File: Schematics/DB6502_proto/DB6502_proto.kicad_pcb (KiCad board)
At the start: 2 copper layers, 133.3 x 105.4 mm, 55 parts, among them J1 System Bus, J10 AVR-ISP-6, J2 Controls, J3 Debug UART, J4 I/O Bus, J5 USB_B, SW1 Reset, U1 DS1813, U2 65C02S, U3 62256, U4 ATmega644PA-PU, U5 62256, U6 74AC138, U7 28C256, U8 22V10C, U9 FT230XS, Y1 20MHz

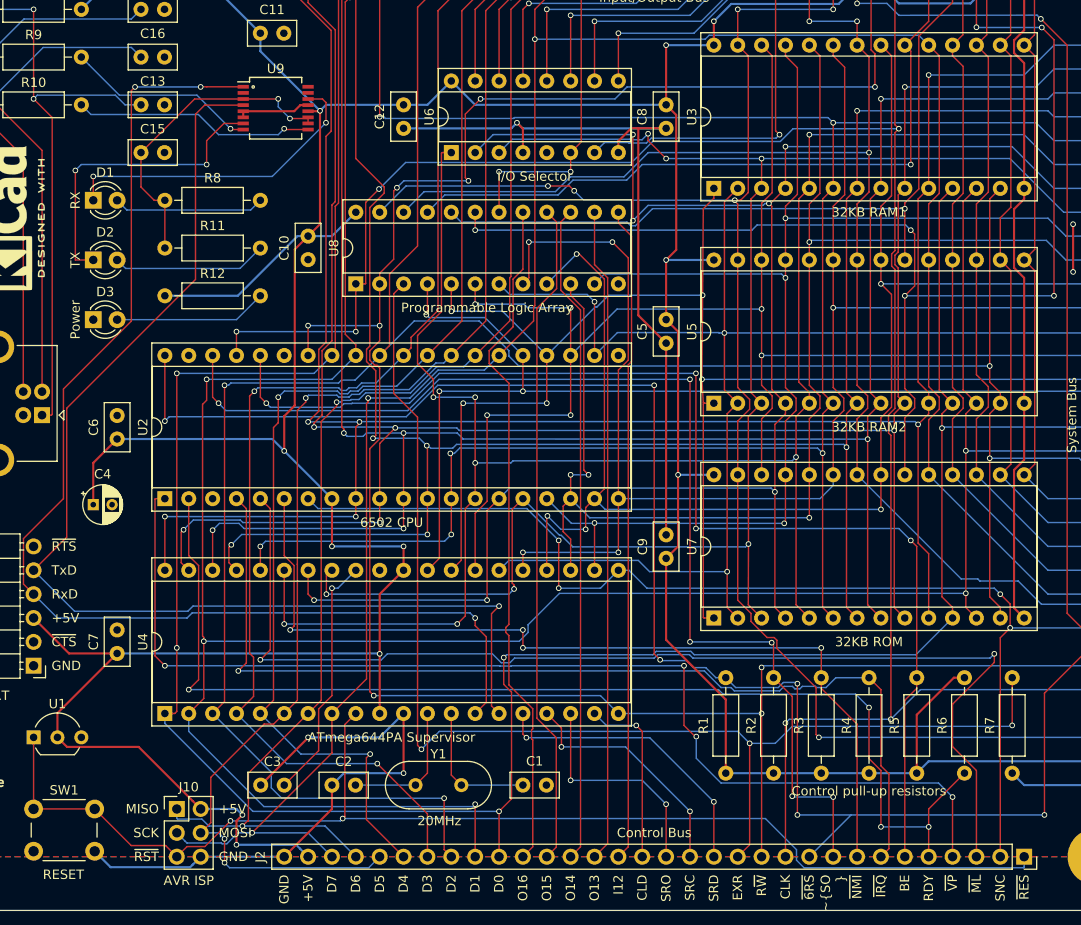
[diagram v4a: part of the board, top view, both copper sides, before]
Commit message: AVR ISP connections cleanup
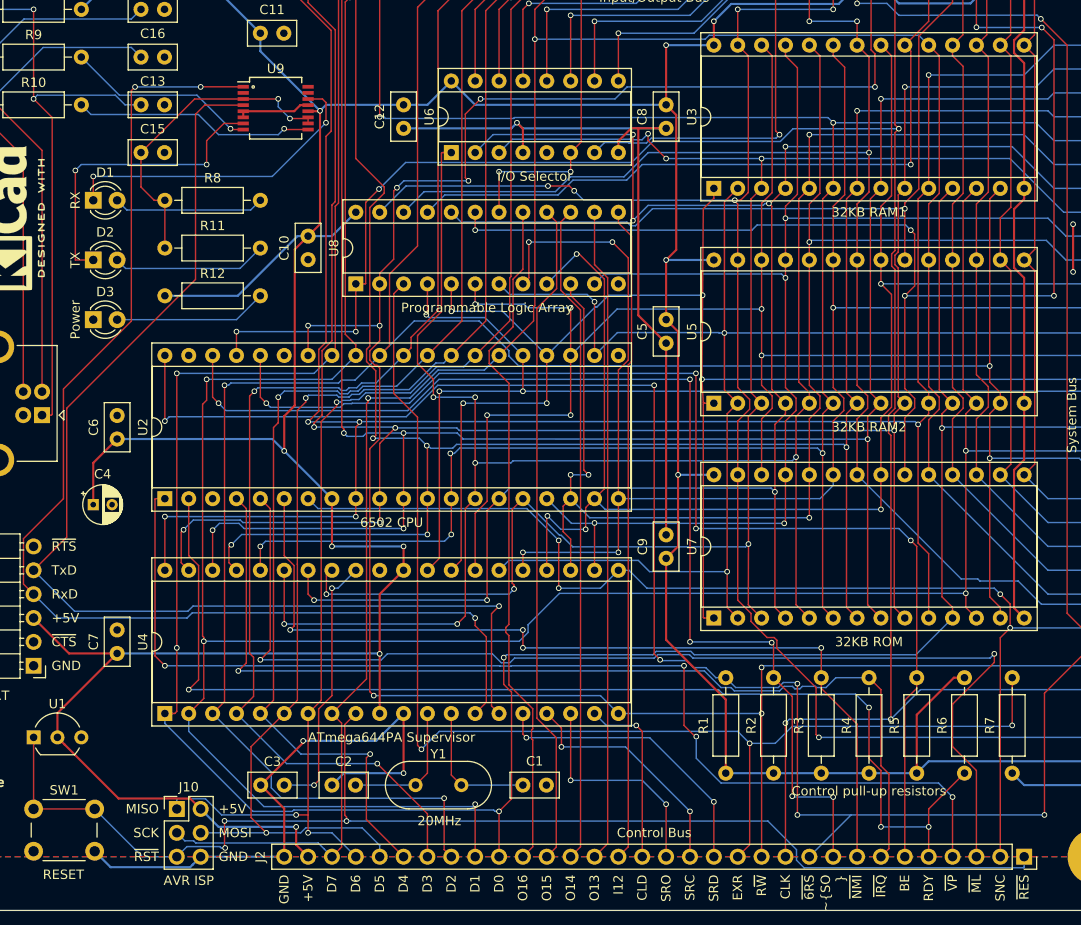
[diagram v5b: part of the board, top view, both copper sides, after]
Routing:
- net d5: track 258.3 -> 254.8 mm, vias 3 -> 2
- net d6: track 252.5 -> 250.4 mm, vias 2 -> 3
- net ~RES: track 132.5 -> 134.5 mm, vias 2 -> 3
- net Net-(C3-Pad2): track 26.4 -> 28.2 mm, vias 1 -> 2
- net +5V: track 470.4 -> 468.7 mm, vias 11 -> 10
- net d7: track 242.7 -> 241.6 mm, vias 3 -> 2
- net GND: track 241.5 -> 240.6 mm

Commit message: Working on the second PCB
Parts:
- removed REF**: OSHW-Logo_7.5x8mm_SilkScreen, Symbol:OSHW-Logo_7.5x8mm_SilkScreen
- removed REF**: KiCad-Logo2_6mm_SilkScreen, Symbol:KiCad-Logo2_6mm_SilkScreen
- removed REF** (x4): MountingHole_3mm_Pad, MountingHole:MountingHole_3mm_Pad
- added C17: 0,1uF, Capacitor_SMD:C_0805_2012Metric_Pad1.15x1.40mm_HandSolder, B.Cu at (449.6, 148.8)
- added C18: 22pF, Capacitor_THT:C_Disc_D5.0mm_W2.5mm_P2.50mm, F.Cu at (337.8, 83.8)
- added C19: 22pF, Capacitor_THT:C_Disc_D5.0mm_W2.5mm_P2.50mm, F.Cu at (360.7, 83.8)
- added C20: 0,1uF, Capacitor_SMD:C_0805_2012Metric_Pad1.15x1.40mm_HandSolder, B.Cu at (96.8, 121.6)
- added C21: 0,1uF, Capacitor_SMD:C_0805_2012Metric_Pad1.15x1.40mm_HandSolder, B.Cu at (62.2, 172.7)
- added C22: 0,1uF, Capacitor_SMD:C_0805_2012Metric_Pad1.15x1.40mm_HandSolder, B.Cu at (62.2, 168.9)
- added C23: 0,1uF, Capacitor_SMD:C_0805_2012Metric_Pad1.15x1.40mm_HandSolder, B.Cu at (363.2, 163.8)
- added C24: 0,1uF, Capacitor_SMD:C_0805_2012Metric_Pad1.15x1.40mm_HandSolder, B.Cu at (437.1, 92.7)
- added C25: 0,1uF, Capacitor_SMD:C_0805_2012Metric_Pad1.15x1.40mm_HandSolder, B.Cu at (363.2, 179.1)
- added C26: 0,1uF, Capacitor_SMD:C_0805_2012Metric_Pad1.15x1.40mm_HandSolder, B.Cu at (96.8, 125.7)
- added C27: 0,1uF, Capacitor_SMD:C_0805_2012Metric_Pad1.15x1.40mm_HandSolder, B.Cu at (378.5, 133.3)
- added C28: 22pF, Capacitor_THT:C_Disc_D5.0mm_W2.5mm_P2.50mm, F.Cu at (454.7, 93.9)
- added C29: 22pF, Capacitor_THT:C_Disc_D5.0mm_W2.5mm_P2.50mm, F.Cu at (454.7, 116.8)
- added C30: 0,1uF, Capacitor_SMD:C_0805_2012Metric_Pad1.15x1.40mm_HandSolder, B.Cu at (378.5, 118.1)
- added D4: BLINK, LED_THT:LED_D3.0mm, F.Cu at (387.4, 143.5)
- added J11: VIA Ports, Connector_PinSocket_2.54mm:PinSocket_1x20_P2.54mm_Vertical, F.Cu at (179.5, 90.8)
- added J12: Power plug, Connector_BarrelJack:BarrelJack_Horizontal, F.Cu at (395.9, 72.4)
- added J6: UART B, Connector_PinHeader_2.54mm:PinHeader_1x06_P2.54mm_Horizontal, F.Cu at (433.1, 68.6)
- added J7: I/O Bus, Connector_PinSocket_2.54mm:PinSocket_1x32_P2.54mm_Vertical, F.Cu at (24.8, 31.0)
- added J8: System Bus, Connector_PinSocket_2.54mm:PinSocket_1x32_P2.54mm_Vertical, F.Cu at (20.2, 31.0)
- added J9: Clock divider, Connector_PinHeader_2.54mm:PinHeader_2x03_P2.54mm_Vertical, F.Cu at (388.6, 152.4)
- added JP1: PLD CLK Selector, Connector_PinSocket_2.54mm:PinSocket_1x03_P2.54mm_Vertical, F.Cu at (378.5, 106.7)
- added JP10: Blink, Connector_PinHeader_2.54mm:PinHeader_2x01_P2.54mm_Vertical, F.Cu at (395.0, 144.8)
- added JP2: PLD ~WR, Connector_PinHeader_2.54mm:PinHeader_1x02_P2.54mm_Vertical, F.Cu at (381.0, 83.8)
- added JP3: PLD ~RD, Connector_PinHeader_2.54mm:PinHeader_1x02_P2.54mm_Vertical, F.Cu at (386.1, 83.8)
- added JP4: PLD RDY, Connector_PinHeader_2.54mm:PinHeader_1x02_P2.54mm_Vertical, F.Cu at (391.2, 83.8)
- added JP5: PLD DBG_WAIT, Connector_PinHeader_2.54mm:PinHeader_1x02_P2.54mm_Vertical, F.Cu at (396.2, 83.8)
- added JP6: PLD WS_DISABLE, Connector_PinHeader_2.54mm:PinHeader_1x02_P2.54mm_Vertical, F.Cu at (401.3, 83.8)
- added JP7: PLD RDY_M1F, Connector_PinHeader_2.54mm:PinHeader_1x02_P2.54mm_Vertical, F.Cu at (406.4, 83.8)
- added JP8: PLD RDY_M2F, Connector_PinHeader_2.54mm:PinHeader_1x02_P2.54mm_Vertical, F.Cu at (411.5, 83.8)
- added JP9: Debug RxD, Connector_PinHeader_2.54mm:PinHeader_2x01_P2.54mm_Vertical, F.Cu at (39.6, 158.2)
- added R13: 27, Resistor_THT:R_Axial_DIN0207_L6.3mm_D2.5mm_P10.16mm_Horizontal, F.Cu at (46.6, 52.1)
- added R14: 27, Resistor_THT:R_Axial_DIN0207_L6.3mm_D2.5mm_P10.16mm_Horizontal, F.Cu at (65.5, 48.1)
- added R15: 220, Resistor_THT:R_Axial_DIN0207_L6.3mm_D2.5mm_P10.16mm_Horizontal, F.Cu at (38.9, 163.2)
- added R16: 220, Resistor_THT:R_Axial_DIN0207_L6.3mm_D2.5mm_P10.16mm_Horizontal, F.Cu at (62.4, 143.7)
- added R17: 4K7, Resistor_THT:R_Axial_DIN0207_L6.3mm_D2.5mm_P10.16mm_Horizontal, F.Cu at (62.4, 147.7)
- added R18: 0R, Resistor_THT:R_Axial_DIN0207_L6.3mm_D2.5mm_P10.16mm_Horizontal, F.Cu at (455.9, 149.9)
- added R19: 220, Resistor_THT:R_Axial_DIN0207_L6.3mm_D2.5mm_P10.16mm_Horizontal, F.Cu at (361.9, 137.2)
- added RV1: 10K, Potentiometer_THT:Potentiometer_Piher_PT-10-V10_Vertical, F.Cu at (386.1, 181.6)
- added TP1: TestPoint, TestPoint:TestPoint_Keystone_5005-5009_Compact, F.Cu at (228.2, 81.7)
- added TP2: TestPoint, TestPoint:TestPoint_Keystone_5005-5009_Compact, F.Cu at (234.8, 76.6)
- added U10: FT230XS, Package_SO:SSOP-16_5.3x6.2mm_P0.65mm, F.Cu at (55.1, 169.2)
- added U11: 74HC595, Package_DIP:DIP-16_W7.62mm_Socket, F.Cu at (378.5, 121.9)
- added U12: 74HC157, Package_DIP:DIP-16_W7.62mm_Socket, F.Cu at (363.2, 152.4)
- added U13: ATmega644PA-PU, Package_DIP:DIP-40_W15.24mm_Socket, F.Cu at (322.6, 106.7)
- added U14: 74AC74, Package_DIP:DIP-14_W7.62mm_Socket, F.Cu at (386.1, 167.6)
- added U15: DS1813, Package_TO_SOT_THT:TO-92_Inline_Wide, F.Cu at (322.6, 73.7)
- added U16: 74AC74, Package_DIP:DIP-14_W7.62mm_Socket, F.Cu at (363.2, 167.6)
- added U17: 74AC08, Package_DIP:DIP-14_W7.62mm_Socket, F.Cu at (403.9, 129.5)
- added U18: SC26C92, Package_LCC:PLCC-44_THT-Socket, F.Cu at (438.1, 97.8)
- added U19: 65C22S, Package_DIP:DIP-40_W15.24mm_Socket, F.Cu at (401.3, 152.4)
- added X1: 8MHz, Oscillator:Oscillator_DIP-14, F.Cu at (363.2, 182.9)
- added Y2: 3,6864MHz, Crystal:Crystal_HC49-U_Vertical, F.Cu at (454.7, 101.6)
- C1, C2: value 22pF -> 0,1uF; footprint Capacitor_THT:C_Disc_D5.0mm_W2.5mm_P2.50mm -> Capacitor_SMD:C_0805_2012Metric_Pad1.15x1.40mm_HandSolder; moved to B.Cu
- C10: value 100nF -> 10uF; footprint Capacitor_THT:C_Disc_D5.0mm_W2.5mm_P2.50mm -> Capacitor_THT:CP_Radial_D4.0mm_P2.00mm
- C11: value 100nF -> 10nF
- C12: value 100nF -> 47pF
- C13: value 10nF -> 47pF
- C14, C16: value 47pF -> 0,1uF; footprint Capacitor_THT:C_Disc_D5.0mm_W2.5mm_P2.50mm -> Capacitor_SMD:C_0805_2012Metric_Pad1.15x1.40mm_HandSolder; moved to B.Cu
- C15, C3, C5, C6, C8, C9: value 100nF -> 0,1uF; footprint Capacitor_THT:C_Disc_D5.0mm_W2.5mm_P2.50mm -> Capacitor_SMD:C_0805_2012Metric_Pad1.15x1.40mm_HandSolder; moved to B.Cu
- C4: value 10uF -> 0,1uF; footprint Capacitor_THT:CP_Radial_D4.0mm_P2.00mm -> Capacitor_SMD:C_0805_2012Metric_Pad1.15x1.40mm_HandSolder; moved to B.Cu
- C7: value 100nF -> 22pF
- D1: value RX -> PWR
- D2: value TX -> D_TX
- D3: value PWR -> D_RX
- J1: value System Bus -> Controls
- J10: value AVR-ISP-6 -> LCD Port; footprint Connector_PinHeader_2.54mm:PinHeader_2x03_P2.54mm_Vertical -> Connector_PinSocket_2.54mm:PinSocket_1x16_P2.54mm_Vertical
- J2: value Controls -> AVR ISP; footprint Connector_PinSocket_2.54mm:PinSocket_1x32_P2.54mm_Vertical -> Connector_PinHeader_2.54mm:PinHeader_2x03_P2.54mm_Vertical
- J3: value Debug UART -> Debug USB; footprint Connector_PinHeader_2.54mm:PinHeader_1x06_P2.54mm_Horizontal -> Connector_USB:USB_B_OST_USB-B1HSxx_Horizontal
- J4: value I/O Bus -> Debug UART; footprint Connector_PinSocket_2.54mm:PinSocket_1x32_P2.54mm_Vertical -> Connector_PinHeader_2.54mm:PinHeader_1x06_P2.54mm_Horizontal
- J5: value USB_B -> UART A; footprint Connector_USB:USB_B_OST_USB-B1HSxx_Horizontal -> Connector_PinHeader_2.54mm:PinHeader_1x06_P2.54mm_Horizontal
- R1: value 4K7 -> 470
- R10, R9: value 27 -> 4K7
- R11, R12, R8: value 220 -> 4K7
- R5: value 4K7 -> 220
- U1: value DS1813 -> 62256; footprint Package_TO_SOT_THT:TO-92_Inline_Wide -> Package_DIP:DIP-28_W15.24mm_Socket
- U2: value 65C02S -> 71256; footprint Package_DIP:DIP-40_W15.24mm_Socket -> Package_DIP:DIP-28_W7.62mm_Socket
- U3: value 62256 -> 71256; footprint Package_DIP:DIP-28_W15.24mm_Socket -> Package_DIP:DIP-28_W7.62mm_Socket
- U4: value ATmega644PA-PU -> 65C02S
- U5: value 62256 -> 74AC74; footprint Package_DIP:DIP-28_W15.24mm_Socket -> Package_DIP:DIP-14_W7.62mm_Socket
- U7: value 28C256 -> 22V10C; footprint Package_DIP:DIP-28_W15.24mm_Socket -> Package_DIP:DIP-24_W7.62mm_Socket
- U8: value 22V10C -> 74AC04; footprint Package_DIP:DIP-24_W7.62mm_Socket -> Package_DIP:DIP-14_W7.62mm_Socket
- U9: value FT230XS -> 74HC21; footprint Package_SO:SSOP-16_5.3x6.2mm_P0.65mm -> Package_DIP:DIP-14_W7.62mm_Socket
- moved C16 376.5 mm to (426.7, 125.7), turned to 270 degrees
- moved J5 359.8 mm to (412.8, 68.6), turned to 90 degrees
- moved J10 353.3 mm to (416.6, 160.0), turned to 90 degrees
- moved C15 346.7 mm to (386.1, 163.8), turned to 270 degrees
- moved U6 343.0 mm to (426.7, 129.5)
- moved U8 334.6 mm to (419.1, 86.4)
- moved C14 325.5 mm to (363.2, 148.6), turned to 270 degrees
- moved D1 325.4 mm to (382.3, 73.1)
- moved C10 324.9 mm to (405.1, 72.4), turned to 0 degrees
- moved C6 318.7 mm to (378.5, 95.2), turned to 270 degrees
- moved U9 318.5 mm to (378.5, 137.2), turned to 90 degrees
- moved J3 316.7 mm to (368.3, 73.7), turned to 90 degrees
- moved C8 295.2 mm to (403.9, 110.5)
- moved C9 288.1 mm to (403.9, 125.7), turned to 270 degrees
- moved U5 284.0 mm to (403.9, 114.3)
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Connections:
- C1 pad 1: GND -> +5V
- C1 pad 2: Net-(C1-Pad2) -> GND
- C11 pad 1: +5V -> Net-(C11-Pad1)
- C12 pad 1: +5V -> Net-(C12-Pad1)
- C14 pad 1: Net-(C14-Pad1) -> +5V
- C15 pad 1: Net-(C15-Pad1) -> +5V
- C16 pad 1: Net-(C16-Pad1) -> +5V
- C2 pad 1: GND -> +5V
- C2 pad 2: Net-(C2-Pad2) -> GND
- C3 pad 1: GND -> +5V
- C3 pad 2: Net-(C3-Pad2) -> GND
- C7 pad 1: +5V -> 6502_RDY_IN
- C7 pad 2: GND -> 6502_RDY
- D1 pad 1: ~RXLED -> GND
- D2 pad 1: ~TXLED -> ~DBG_TXLED
- D3 pad 1: GND -> ~DBG_RXLED
- FB1 pad 2: Net-(C13-Pad1) -> Net-(C11-Pad1)
- J1 pad 1: a0 -> ~RES
- J1 pad 10: a9 -> ~6502_RES
- J1 pad 11: a10 -> 6502_CLK
- J1 pad 12: a11 -> R~W
- J1 pad 13: a12 -> EXRAM
- J1 pad 14: a13 -> SR_DAT
- J1 pad 15: a14 -> SR_CLK
- J1 pad 16: a15 -> SR_OUT
- J1 pad 17: d0 -> DBG_CLK
- J1 pad 18: d1 -> RDY_M1F
- J1 pad 19: d2 -> RDY_M2F
- J1 pad 2: a1 -> SYNC
- J1 pad 20: d3 -> WS_DISABLE
- J1 pad 21: d4 -> DBG_WAIT
- J1 pad 22: d5 -> 6502_RDY
- J1 pad 23: d6 -> d0
- J1 pad 24: d7 -> d1
- J1 pad 25: SYNC -> d2
- J1 pad 26: ~6502_RES -> d3
- J1 pad 27: R~W -> d4
- J1 pad 28: CLK -> d5
- J1 pad 29: ~OE -> d6
- J1 pad 3: a2 -> ~ML
- J1 pad 30: ~WE -> d7
- J1 pad 4: a3 -> ~VP
- J1 pad 5: a4 -> 6502_RDY
- J1 pad 6: a5 -> BE
- J1 pad 7: a6 -> ~IRQ
- J1 pad 8: a7 -> ~NMI
- J1 pad 9: a8 -> ~SO
- J10 pad 1: d6 -> GND
- J10 pad 3: d7 -> Net-(J10-Pad3)
- J10 pad 4: d5 -> /serial/v1pb1
- J10 pad 5: ~RES -> /serial/v1pb2
- J10 pad 6: GND -> /serial/v1pb3
- J2 pad 1: ~RES -> d6
- J2 pad 2: SYNC -> +5V
- J2 pad 3: ~ML -> d7
- J2 pad 4: ~VP -> d5
- J2 pad 5: RDY -> ~RES
- J2 pad 6: BE -> GND
- J3 pad 1: GND -> Net-(C11-Pad1)
- J3 pad 2: GND -> Net-(C13-Pad1)
- J3 pad 3: +5V -> Net-(C12-Pad1)
- J3 pad 4: RxD_DBG -> GND
- J3 pad 5: TxD_DBG -> Net-(J3-Pad5)
- J4 pad 1: a0 -> GND
- J4 pad 2: a1 -> GND
- J4 pad 3: a2 -> Net-(J4-Pad3)
- J4 pad 4: a3 -> DBG_RxD
- J4 pad 5: a4 -> DBG_TxD
- J4 pad 6: d0 -> Net-(J4-Pad6)
- J5 pad 1: Net-(C13-Pad1) -> GND
- J5 pad 2: Net-(C16-Pad1) -> UART_A_~RTS
- J5 pad 3: Net-(C14-Pad1) -> Net-(J5-Pad3)
- J5 pad 4: GND -> UART_A_RxD
- J5 pad 5: Net-(J5-Pad5) -> UART_A_TxD
- R1 pad 1: +5V -> 6502_RDY_IN
- R1 pad 2: ~6502_RES -> 6502_RDY
- R10 pad 1: Net-(C16-Pad1) -> +5V
- R10 pad 2: USBD- -> BE
- R11 pad 1: Net-(C15-Pad1) -> 6502_RDY
- R11 pad 2: Net-(D2-Pad2) -> +5V
- R12 pad 1: +5V -> GND
- R12 pad 2: Net-(D3-Pad2) -> EXRAM
- R2 pad 2: ~SO -> ~EXT_IRQ
- R3 pad 2: ~NMI -> ~UART_IRQ
- R4 pad 2: ~IRQ -> ~VIA2_IRQ
- R5 pad 2: BE -> Net-(D1-Pad2)
- R6 pad 1: RDY -> +5V
- R6 pad 2: +5V -> ~6502_RES
- R7 pad 1: GND -> +5V
- R7 pad 2: EXRAM -> ~SO
- R8 pad 1: Net-(C15-Pad1) -> +5V
- R8 pad 2: Net-(D1-Pad2) -> ~NMI
- R9 pad 1: Net-(C14-Pad1) -> +5V
- R9 pad 2: USBD+ -> ~IRQ
- U1 pad 1: ~RES -> a14
- U1 pad 2: +5V -> a12
- U1 pad 3: GND -> a7
- U2 pad 1: ~VP -> a14
- U2 pad 10: a1 -> a0
- U2 pad 11: a2 -> d0
- U2 pad 12: a3 -> d1
- U2 pad 13: a4 -> d2
- U2 pad 14: a5 -> GND
- U2 pad 15: a6 -> d3
- U2 pad 16: a7 -> d4
- U2 pad 17: a8 -> d5
- U2 pad 18: a9 -> d6
- U2 pad 19: a10 -> d7
- U2 pad 2: RDY -> a12
- U2 pad 20: a11 -> RAM2_~CS
- U2 pad 21: GND -> a10
- U2 pad 22: a12 -> ~RD
- U2 pad 23: a13 -> a11
- U2 pad 24: a14 -> a9
- U2 pad 25: a15 -> a8
- U2 pad 26: d7 -> a13
- U2 pad 27: d6 -> ~WR
- U2 pad 28: d5 -> +5V
- U2 pad 3: Net-(U2-Pad3) -> a7
- U2 pad 4: ~IRQ -> a6
- U2 pad 5: ~ML -> a5
- U2 pad 6: ~NMI -> a4
- U2 pad 7: SYNC -> a3
- U2 pad 8: +5V -> a2
- U2 pad 9: a0 -> a1
- U3 pad 20: RAM1_~CS -> ROM_~CS
- U3 pad 22: ~OE -> ~RD
- U3 pad 27: ~WE -> ~WR
- U4 pad 1: d0 -> ~VP
- U4 pad 10: +5V -> a1
- U4 pad 11: GND -> a2
- U4 pad 12: Net-(C2-Pad2) -> a3
- U4 pad 13: Net-(C1-Pad2) -> a4
- U4 pad 14: RxD_DBG -> a5
- U4 pad 15: TxD_DBG -> a6
- U4 pad 16: SR_DAT -> a7
- U4 pad 17: SR_CLK -> a8
- U4 pad 18: SR_OUT -> a9
- U4 pad 19: CLK_DBG -> a10
- U4 pad 2: d1 -> 6502_RDY_IN
- U4 pad 20: R~W -> a11
- U4 pad 21: SYNC -> GND
- U4 pad 22: a8 -> a12
- U4 pad 23: a9 -> a13
- U4 pad 24: a10 -> a14
- U4 pad 25: a11 -> a15
- U4 pad 26: a12 -> d7
- U4 pad 27: a13 -> d6
- U4 pad 28: a14 -> d5
- U4 pad 29: a15 -> d4
- U4 pad 3: d2 -> Net-(U4-Pad3)
- U4 pad 30: +5V -> d3
- U4 pad 31: GND -> d2
- U4 pad 32: Net-(C3-Pad2) -> d1
- U4 pad 33: a7 -> d0
- U4 pad 34: a6 -> R~W
- U4 pad 35: a5 -> Net-(U4-Pad35)
- U4 pad 36: a4 -> BE
- U4 pad 37: a3 -> 6502_CLK
- U4 pad 38: a2 -> ~SO
- U4 pad 39: a1 -> Net-(U4-Pad39)
- U4 pad 4: d3 -> ~IRQ
- U4 pad 40: a0 -> ~6502_RES
- U4 pad 5: d4 -> ~ML
- U4 pad 6: d5 -> ~NMI
- U4 pad 7: d6 -> SYNC
- U4 pad 8: d7 -> +5V
- U4 pad 9: ~RES -> a0
- U5 pad 1: a14 -> +5V
- U5 pad 10: a0 -> ~6502_RES
- U5 pad 11: d0 -> ~6502_CLK
- U5 pad 12: d1 -> RDY_M1F
- U5 pad 13: d2 -> +5V
- U5 pad 14: GND -> +5V
- U5 pad 2: a12 -> 6502_RDY
- U5 pad 3: a7 -> ~6502_CLK
- U5 pad 4: a6 -> ~6502_RES
- U5 pad 5: a5 -> RDY_M1F
- U5 pad 6: a4 -> Net-(U5-Pad6)
- U5 pad 7: a3 -> GND
- U5 pad 8: a2 -> Net-(U5-Pad8)
- U5 pad 9: a1 -> RDY_M2F
- U7 pad 1: a14 -> PLD_CLK
- U7 pad 10: a0 -> a9
- U7 pad 11: d0 -> a8
- U7 pad 12: d1 -> GND
- U7 pad 13: d2 -> IN12
- U7 pad 14: GND -> IO13
- U7 pad 15: d3 -> IO14
- U7 pad 16: d4 -> IO15
- U7 pad 17: d5 -> IO16
- U7 pad 18: d6 -> IOCS
- U7 pad 19: d7 -> ROM_~CS
- U7 pad 2: a12 -> R~W
- U7 pad 20: ROM_~CS -> RAM2_~CS
- U7 pad 21: a10 -> RAM1_~CS
- U7 pad 22: ~OE -> ~PLD_RD
- U7 pad 23: a11 -> ~PLD_WR
- U7 pad 24: a9 -> +5V
- U7 pad 3: a7 -> EXRAM
- U7 pad 4: a6 -> a15
- U7 pad 5: a5 -> a14
- U7 pad 6: a4 -> a13
- U7 pad 7: a3 -> a12
- U7 pad 8: a2 -> a11
- U7 pad 9: a1 -> a10
- U8 pad 10: a9 -> UART_RES
- U8 pad 11: a8 -> ~6502_RES
- U8 pad 12: GND -> ~6502_CLK
- U8 pad 13: IN12 -> 6502_CLK_IN
- U8 pad 14: IO13 -> +5V
- U8 pad 2: R~W -> ~CLK
- U8 pad 3: EXRAM -> ~DBG_BE
- U8 pad 4: a15 -> BE
- U8 pad 5: a14 -> DBG_RES
- U8 pad 6: a13 -> ~DBG_RES
- U8 pad 7: a12 -> GND
- U8 pad 8: a11 -> 6502_CLK
- U8 pad 9: a10 -> ~6502_CLK
- U9 pad 1: RxD_DBG -> ~VIA1_IRQ
- U9 pad 10: Net-(C15-Pad1) -> GND
- U9 pad 11: Net-(C15-Pad1) -> (no net)
- U9 pad 12: +5V -> GND
- U9 pad 14: ~RXLED -> +5V
- U9 pad 2: Net-(U9-Pad2) -> ~VIA2_IRQ
- U9 pad 3: Net-(C15-Pad1) -> (no net)
- U9 pad 4: TxD_DBG -> ~UART_IRQ
- U9 pad 5: GND -> ~EXT_IRQ
- U9 pad 6: GND -> ~IRQ
- U9 pad 7: ~TXLED -> GND
- U9 pad 8: USBD+ -> Net-(U9-Pad8)
- U9 pad 9: USBD- -> GND
- Y1 pad 1: Net-(C1-Pad2) -> Net-(C18-Pad2)
- Y1 pad 2: Net-(C2-Pad2) -> Net-(C19-Pad2)
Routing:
- net +5V: track 468.7 -> 0.00 mm, vias 10 -> 0
- net d1: track 288.2 -> 0.00 mm, vias 6 -> 0
- net d0: track 279.1 -> 0.00 mm, vias 6 -> 0
- net ~6502_RES: track 265.6 -> 0.00 mm, vias 8 -> 0
- net d2: track 261.3 -> 0.00 mm, vias 4 -> 0
- net d5: track 254.8 -> 0.00 mm, vias 2 -> 0
- net d3: track 252.5 -> 0.00 mm, vias 2 -> 0
- net d6: track 250.4 -> 0.00 mm, vias 3 -> 0
- net d4: track 246.8 -> 0.00 mm, vias 2 -> 0
- net d7: track 241.6 -> 0.00 mm, vias 2 -> 0
- net GND: track 240.6 -> 0.00 mm, vias 5 -> 0
- net R~W: track 237.7 -> 0.00 mm, vias 9 -> 0
- net a0: track 230.9 -> 0.00 mm, vias 6 -> 0
- net a1: track 228.6 -> 0.00 mm, vias 6 -> 0
- net a2: track 221.5 -> 0.00 mm, vias 6 -> 0
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- removed copper zone on B.Cu, net GND
- removed copper zone on F.Cu, net GND
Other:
- board outline removed
- board text added: "DBG"
- board text added: "M1F"
- board text added: "M2F"
- board text added: "WSD"
- board text added: "~CLK"
- board text added: "~RD"
- board text added: "~WR"
- board text removed: "+5V"
- board text removed: "20MHz"
- board text removed: "32KB RAM1"
- board text removed: "32KB RAM2"
- board text removed: "32KB ROM"
- board text removed: "6502 CPU"
- board text removed: "6502 Prototype Board Designed by Dawid Buchwald https://github.com/dbuchwald/6502"
- board text removed: "A00"
- board text removed: "A01"
- board text removed: "A02"
- board text removed: "A03"
- board text removed: "A04"
- board text removed: "A05"
- board text removed: "A06"
- board text removed: "A07"
- board text removed: "A08"
- board text removed: "A09"
- board text removed: "A10"
- board text removed: "A11"
- board text removed: "A12"
- board text removed: "A13"
- board text removed: "A14"
- board text removed: "A15"
- board text removed: "ATmega644PA Supervisor"
- board text removed: "AVR ISP"
- board text removed: "BE"
- board text removed: "CLD"
- board text removed: "Control Bus"
- board text removed: "Control pull-up resistors"
- board text removed: "D0"
- board text removed: "D1"
- board text removed: "D2"
- board text removed: "D3"
- board text removed: "D4"
- board text removed: "D5"
- board text removed: "D6"
- board text removed: "D7"
- board text removed: "EXR"
- board text removed: "GND"
- board text removed: "I/O Selector"
- board text removed: "I12"
- board text removed: "IO"
- board text removed: "Input/Output Bus"
- board text removed: "MISO"
- board text removed: "MOSI"
- board text removed: "O13"
- board text removed: "O14"
- board text removed: "O15"
- board text removed: "O16"
- board text removed: "Power"
- board text removed: "Programmable Logic Array"
- board text removed: "RESET"
- board text removed: "RX"
- board text removed: "RxD"
- board text removed: "R~W"
- board text removed: "SCK"
- board text removed: "SNC"
- board text removed: "SRC"
- board text removed: "SRD"
- board text removed: "SRO"
- board text removed: "System Bus"
- board text removed: "TX"
- board text removed: "TxD"
- board text removed: "UART"
- board text removed: "USB"
- board text removed: "~6RS"
- board text removed: "~CTS"
- board text removed: "~IO0"
- board text removed: "~IO1"
- board text removed: "~IO2"
- board text removed: "~IO3"
- board text removed: "~IRQ"
- board text removed: "~LAT"
- board text removed: "~ML"
- board text removed: "~NMI"
- board text removed: "~OE"
- board text removed: "~RES"
- board text removed: "~RM1"
- board text removed: "~RM2"
- board text removed: "~ROM"
- board text removed: "~RST"
- board text removed: "~RTS"
- board text removed: "~SO"
- board text removed: "~URT"
- board text removed: "~VI1"
- board text removed: "~VI2"
- board text removed: "~VP"
- board text removed: "~WE"

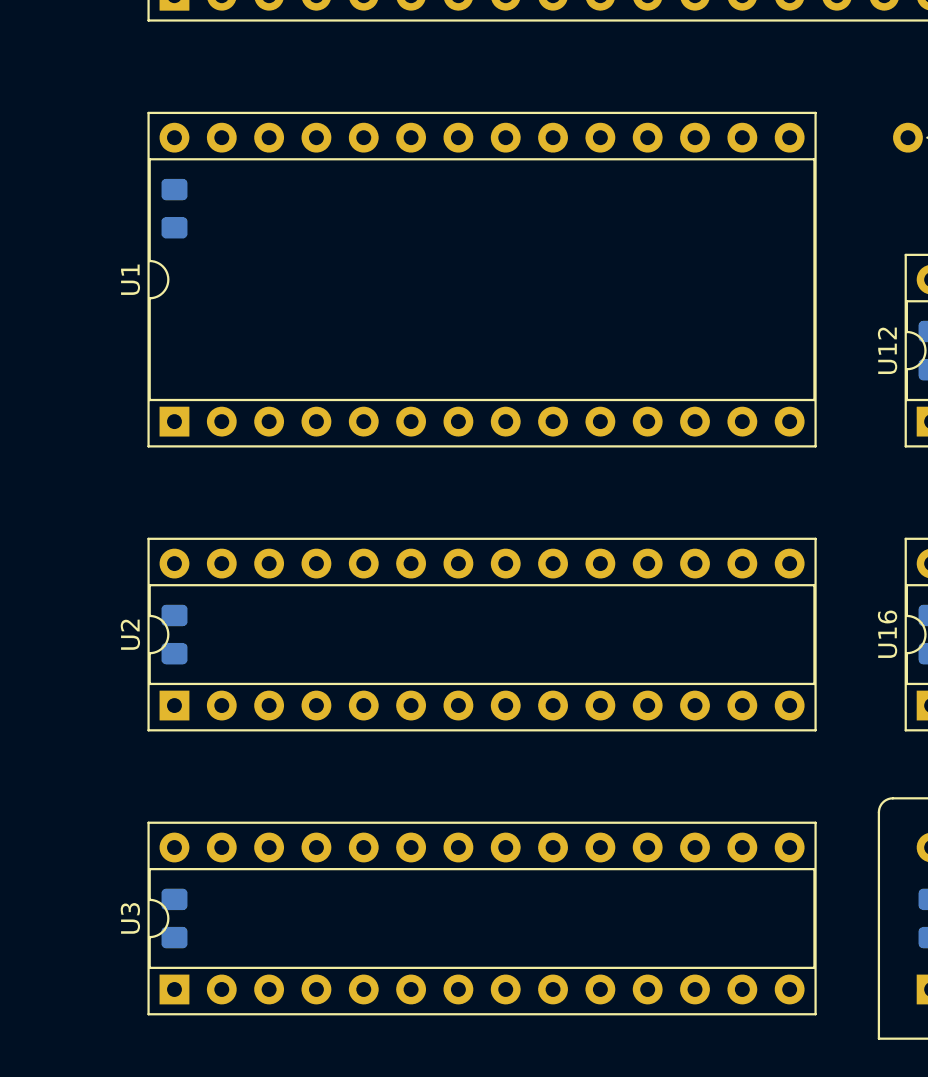
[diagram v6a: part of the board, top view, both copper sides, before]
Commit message: Updated RAM/ROM footprints
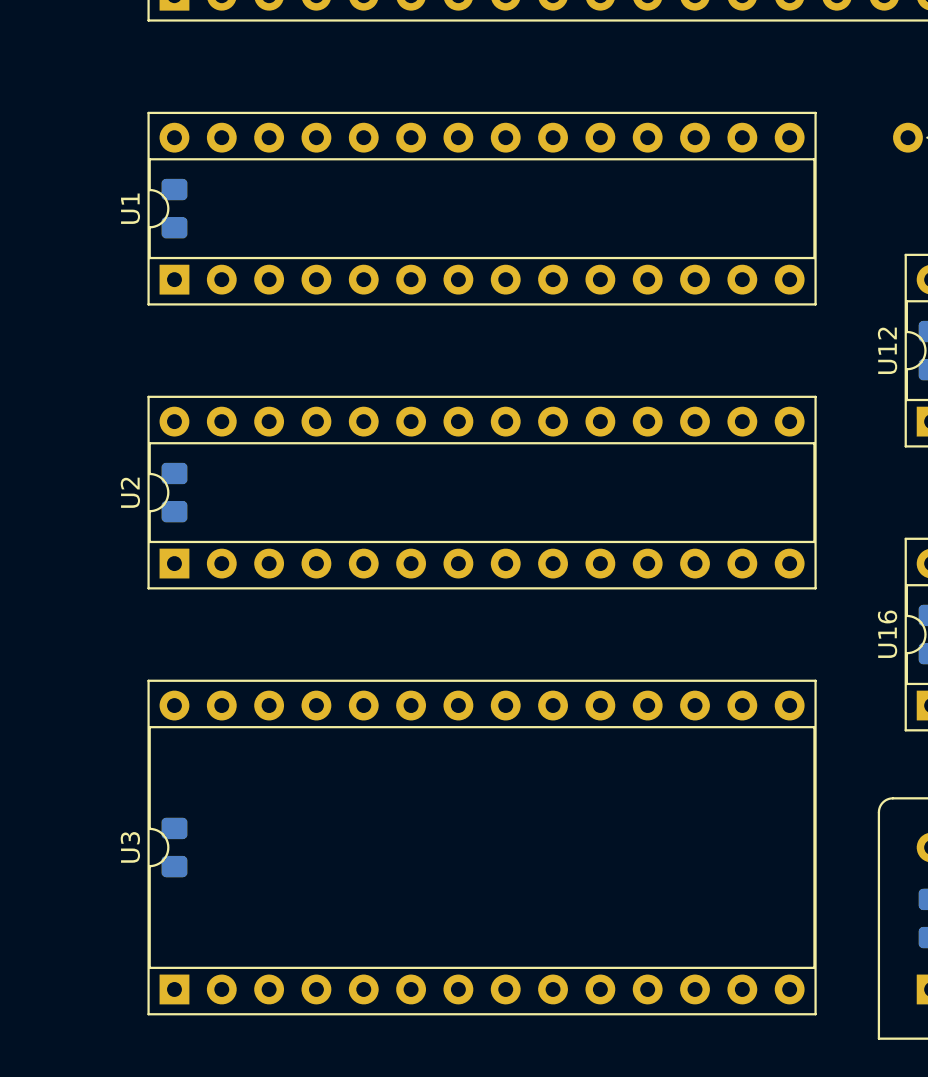
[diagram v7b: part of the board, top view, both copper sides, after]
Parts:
- U1: value 62256 -> 71256; footprint Package_DIP:DIP-28_W15.24mm_Socket -> Package_DIP:DIP-28_W7.62mm_Socket
- U3: value 71256 -> 28C256; footprint Package_DIP:DIP-28_W7.62mm_Socket -> Package_DIP:DIP-28_W15.24mm_Socket
- moved C4 7.62 mm to (322.6, 156.2)
- moved U1 7.62 mm to (322.6, 144.8)
- moved U2 7.62 mm to (322.6, 160.0)
- moved C5 3.81 mm to (322.6, 175.3)

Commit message: Working on a PCB - first traces routed
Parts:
- C14, C15, C16, C23, C26, C27, C30, C8, C9: moved to F.Cu
- U11, U12, U6: footprint Package_DIP:DIP-16_W7.62mm_Socket -> Package_SO:SOIC-16_3.9x9.9mm_P1.27mm
- U14, U16, U17, U5, U8, U9: footprint Package_DIP:DIP-14_W7.62mm_Socket -> Package_SO:SOIC-14_3.9x8.7mm_P1.27mm
- moved J11 320.6 mm to (487.7, 179.1), turned to 90 degrees
- moved JP9 314.5 mm to (342.9, 74.9)
- moved C26 309.7 mm to (403.9, 166.1), turned to 90 degrees
- moved C20 227.3 mm to (322.6, 95.0), turned to 270 degrees
- moved R19 113.5 mm to (471.8, 165.7)
- moved U19 88.7 mm to (487.7, 172.7)
- moved C17 88.7 mm to (535.9, 168.9)
- moved JP10 88.1 mm to (482.0, 158.8), turned to 180 degrees
- moved D4 85.8 mm to (471.8, 158.8)
- moved RV1 85.8 mm to (471.8, 177.8)
- moved U8 80.4 mm to (411.5, 166.4)
- moved R18 78.4 mm to (525.8, 185.4), turned to 0 degrees
- moved J10 70.8 mm to (482.6, 185.4)
- moved U12 67.5 mm to (429.3, 166.4)
- moved U5 64.0 mm to (411.5, 177.8)
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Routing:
- net a12: track 0.00 -> 145.4 mm, vias 0 -> 3
- net a14: track 0.00 -> 138.9 mm, vias 0 -> 3
- net a7: track 0.00 -> 138.3 mm, vias 0 -> 3
- net a6: track 0.00 -> 131.6 mm, vias 0 -> 3
- net a13: track 0.00 -> 127.2 mm, vias 0 -> 4
- net a5: track 0.00 -> 126.1 mm, vias 0 -> 3
- net a4: track 0.00 -> 122.2 mm, vias 0 -> 2
- net a3: track 0.00 -> 121.9 mm, vias 0 -> 3
- net a11: track 0.00 -> 120.6 mm, vias 0 -> 4
- net a2: track 0.00 -> 120.3 mm, vias 0 -> 4
- net a1: track 0.00 -> 118.0 mm, vias 0 -> 4
- net a0: track 0.00 -> 114.2 mm, vias 0 -> 2
- net a8: track 0.00 -> 113.2 mm, vias 0 -> 3
- net a9: track 0.00 -> 110.4 mm, vias 0 -> 2
- net a10: track 0.00 -> 108.5 mm, vias 0 -> 3
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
